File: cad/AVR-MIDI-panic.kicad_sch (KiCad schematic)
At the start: 17 parts, among them J1 MIDI-OUT, J2 MIDI-IN, SW1 B, SW2 A, SW3 LOCK, U1 ATtiny13-20P, U2 6N136

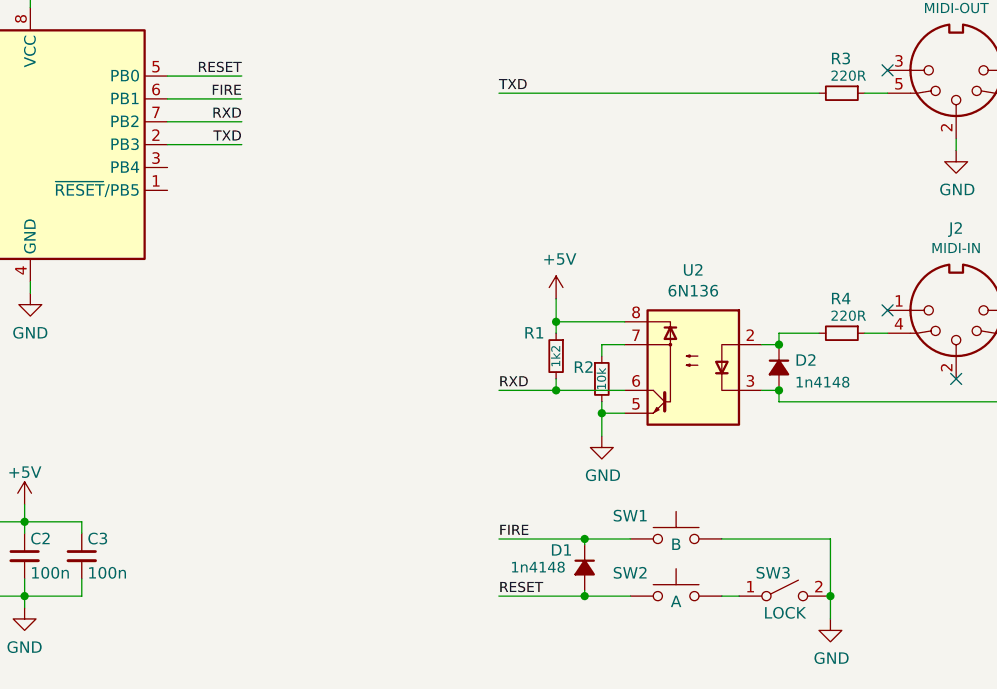
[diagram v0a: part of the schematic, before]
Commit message: Wrong switch assignation
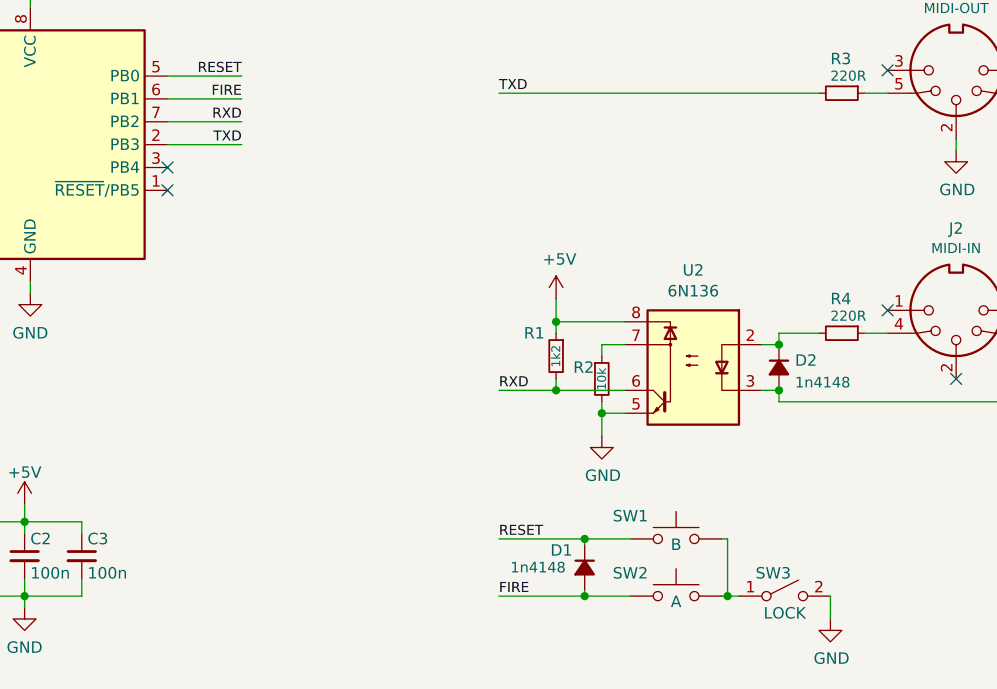
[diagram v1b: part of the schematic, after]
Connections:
- net FIRE: now also D1.2 (A), SW2.1; no longer D1.1 (K), SW1.1
- net GND: no longer SW1.2
- net RESET: now also D1.1 (K), SW1.1; no longer D1.2 (A), SW2.1
- net at SW2.2, SW3.1 (A): now also SW1.2
- no-connect marks 5 -> 7
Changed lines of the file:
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@@
   (junction (at 165.1 113.665) (diameter 0) (color 0 0 0 0)
   )
+  (junction (at 180.975 113.665) (diameter 0) (color 0 0 0 0)
+  )
   (junction (at 102.87 105.41) (diameter 0) (color 0 0 0 0)
   )
   (junction (at 161.925 83.185) (diameter 0) (color 0 0 0 0)
-  )
-  (junction (at 192.405 113.665) (diameter 0) (color 0 0 0 0)
   )
   (junction (at 102.87 113.665) (diameter 0) (color 0 0 0 0)
@@
   (no_connect (at 198.755 55.245))
   (no_connect (at 213.995 81.915))
+  (no_connect (at 118.745 66.04))
+  (no_connect (at 118.745 68.58))
   (no_connect (at 198.755 81.915))
   (wire (pts (xy 184.785 85.725) (xy 186.69 85.725))
     (stroke (width 0) (type default) (color 0 0 0 0))
   )
+  (wire (pts (xy 180.34 107.315) (xy 180.975 107.315))
+    (stroke (width 0) (type default) (color 0 0 0 0))
+  )
   (wire (pts (xy 118.745 60.96) (xy 127 60.96))
     (stroke (width 0) (type default) (color 0 0 0 0))
@@
     (stroke (width 0) (type default) (color 0 0 0 0))
   )
-  (wire (pts (xy 192.405 107.315) (xy 180.34 107.315))
-    (stroke (width 0) (type default) (color 0 0 0 0))
-  )
   (wire (pts (xy 165.1 113.665) (xy 155.575 113.665))
     (stroke (width 0) (type default) (color 0 0 0 0))
@@
     (stroke (width 0) (type default) (color 0 0 0 0))
   )
+  (wire (pts (xy 180.975 113.665) (xy 182.245 113.665))
+    (stroke (width 0) (type default) (color 0 0 0 0))
+  )
   (wire (pts (xy 155.575 107.315) (xy 165.1 107.315))
     (stroke (width 0) (type default) (color 0 0 0 0))
@@
     (stroke (width 0) (type default) (color 0 0 0 0))
   )
-  (wire (pts (xy 180.34 113.665) (xy 182.245 113.665))
-    (stroke (width 0) (type default) (color 0 0 0 0))
-  )
-  (wire (pts (xy 192.405 113.665) (xy 192.405 107.315))
+  (wire (pts (xy 180.34 113.665) (xy 180.975 113.665))
     (stroke (width 0) (type default) (color 0 0 0 0))
   )
@@
   )
   (wire (pts (xy 96.52 113.665) (xy 102.87 113.665))
+    (stroke (width 0) (type default) (color 0 0 0 0))
+  )
+  (wire (pts (xy 180.975 107.315) (xy 180.975 113.665))
     (stroke (width 0) (type default) (color 0 0 0 0))
   )
@@
     (effects (font (size 1.1176 1.1176)) (justify right bottom))
   )
-  (label "RESET" (at 155.575 113.665 0)
+  (label "RESET" (at 155.575 107.315 0)
     (effects (font (size 1.1176 1.1176)) (justify left bottom))
   )
@@
     (effects (font (size 1.1176 1.1176)) (justify left bottom))
   )
-  (label "FIRE" (at 155.575 107.315 0)
-    (effects (font (size 1.1176 1.1176)) (justify left bottom))
-  )
+  (label "FIRE" (at 155.575 113.665 0)
+    (effects (font (size 1.1176 1.1176)) (justify left bottom))
+  )

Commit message: Add reset and tx Led
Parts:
- added D3: tx, symbol Device:LED_Small_Filled
- added R6: 4k7, symbol Device:R_Small
- added R7: 470R, symbol Device:R_Small
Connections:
- net +5V: now also R6.1
- net GND: now also D3.1 (K)
- net RESET: now also U1.1 (~{RESET}/PB5), R6.2
- net LED: now reaches U1.3 (PB4)
- net LED: now also R7.2
- new net: D3.2 (A), R7.1
- no-connect marks 7 -> 5
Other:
- moved on the sheet: C1, C2, C3, D1, D2, J1, J2, R1, R2, R3, R4, R5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

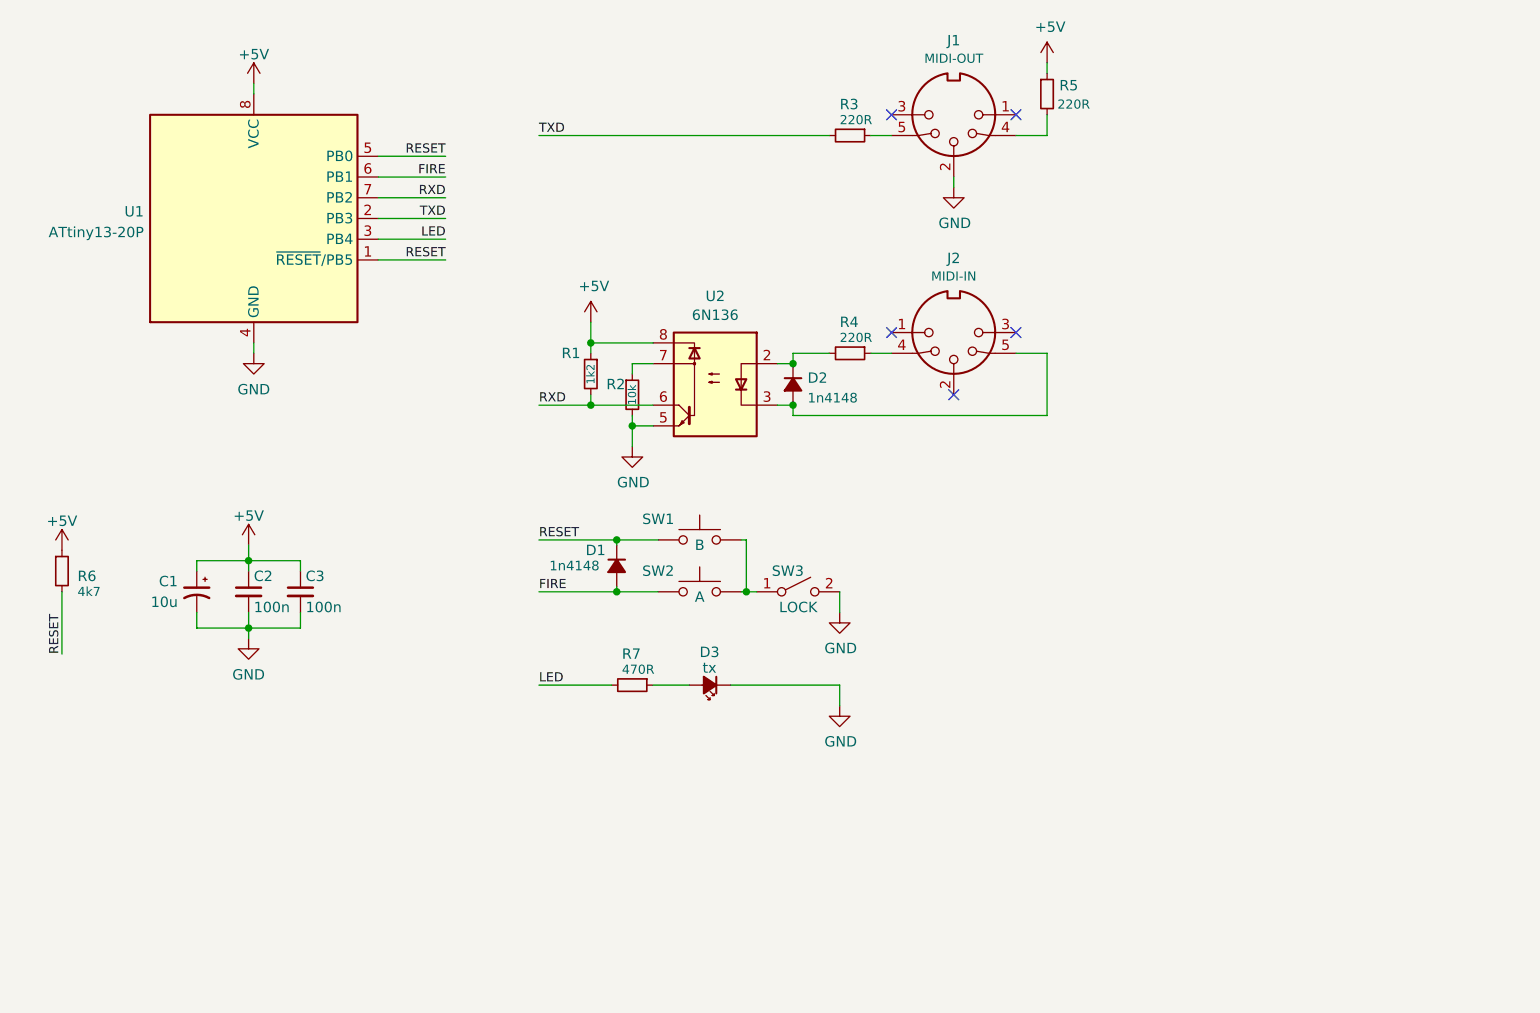
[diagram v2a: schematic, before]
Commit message: Fix double RESET label, Add R to RST switch.
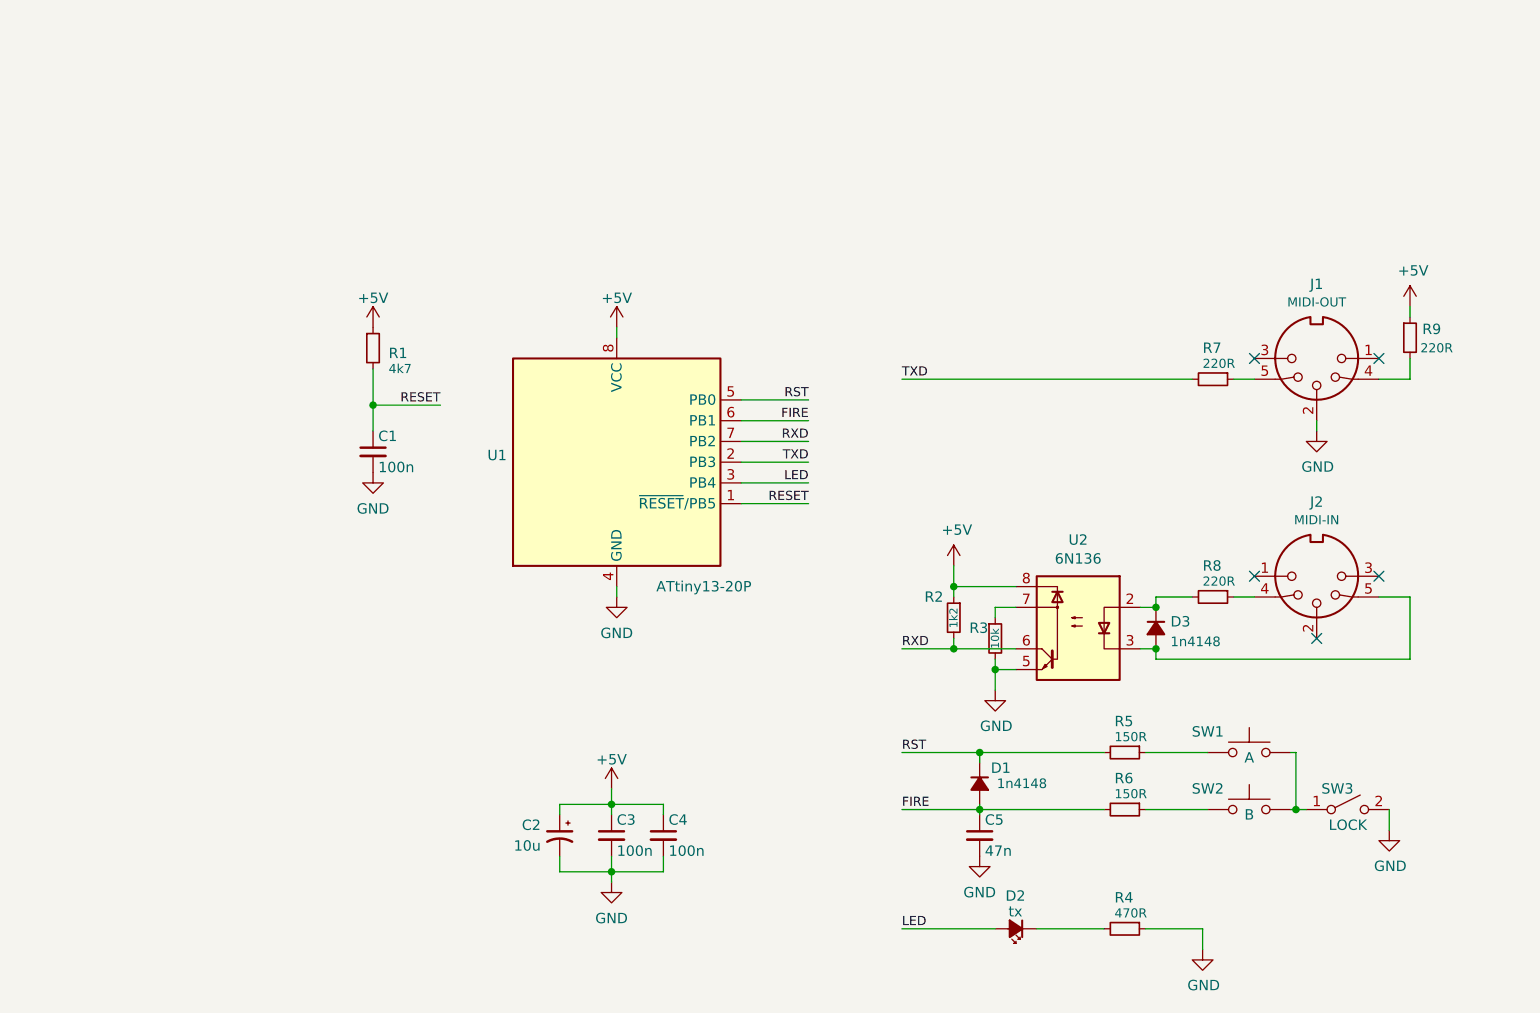
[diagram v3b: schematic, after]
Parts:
- added C1: 100n, symbol Device:C_Small
- added C5: 47n, symbol Device:C_Small
- added R5, R6: 150R, symbol Device:R_Small
- SW1: value B -> A
- SW2: value A -> B
- renumbered C1 to C2, C2 to C3, C3 to C4, D3 to D2, D2 to D3, R6 to R1, R1 to R2, R2 to R3, R7 to R4, R3 to R7, R4 to R8, R5 to R9
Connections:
- net FIRE: now also C5.1, R6.2; no longer SW2.1
- net GND: now also R4.1, C1.2, C5.2; no longer D2.1 (K)
- net LED: now also D2.2 (A); no longer R4.2
- net RESET: now also C1.1; no longer D1.1 (K), SW1.1, U1.5 (PB0)
- new net: D2.1 (K), R4.2
- new net: R6.1, SW2.1
- new net: R5.1, SW1.1
- new net RST: D1.1 (K), R5.2, U1.5 (PB0)
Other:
- moved on the sheet: C2, C3, C4, D2, D3, J1, J2, R1, R2, R3, R4, R7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
